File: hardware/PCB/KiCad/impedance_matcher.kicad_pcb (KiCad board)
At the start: 2 copper layers, 72 x 63 mm, 43 parts, among them Q1 PC817, U1 TLV2372IP

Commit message: Small PCB fixes
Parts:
- FAN1, OLED1: footprint Connector:B4B-XH-A -> Project Connectors:B4B-XH-A
- I2C1: footprint Connector:B2B-XH-A -> Project Connectors:B2B-XH-A
- SWR1: footprint Connector:B3B-XH-A -> Project Connectors:B3B-XH-A
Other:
- board text added: "FAN1"
- board text added: "I2C1"
- board text added: "OLED1"
- board text added: "SWR1"

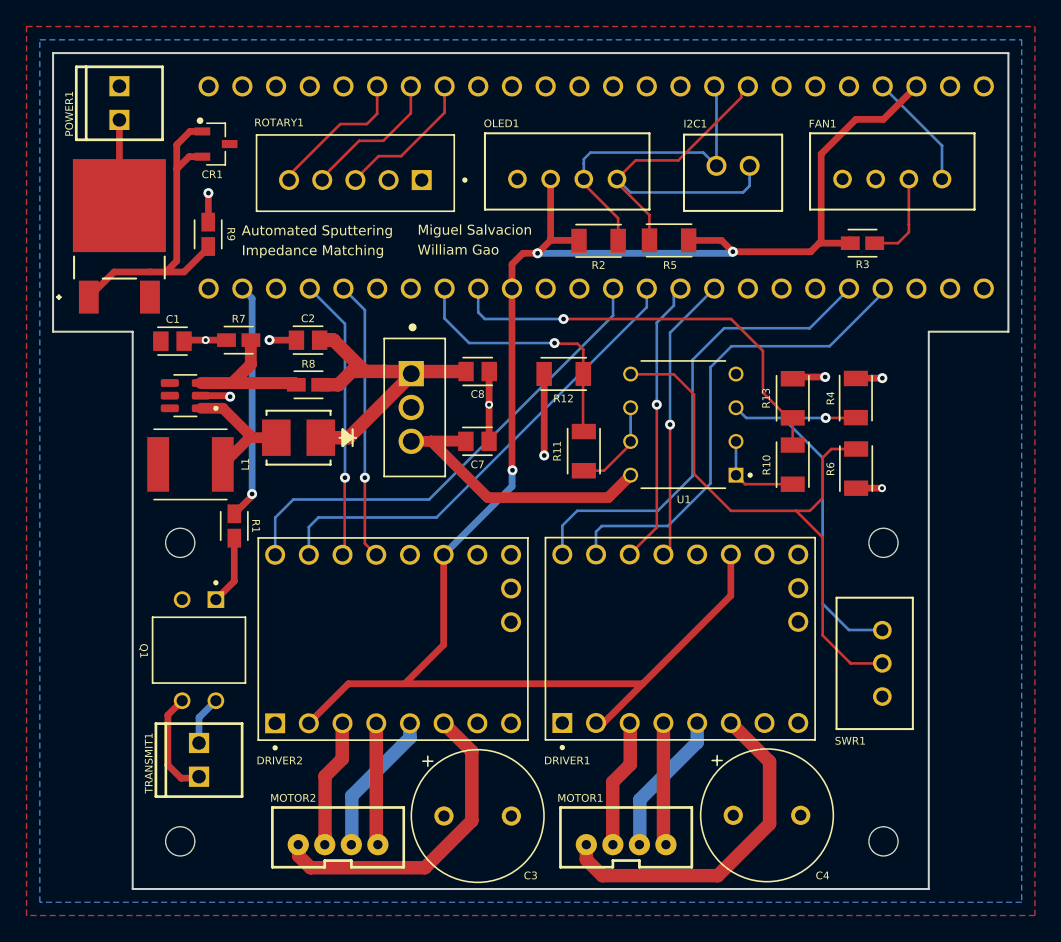
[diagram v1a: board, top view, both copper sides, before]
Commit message: Add some 3D models
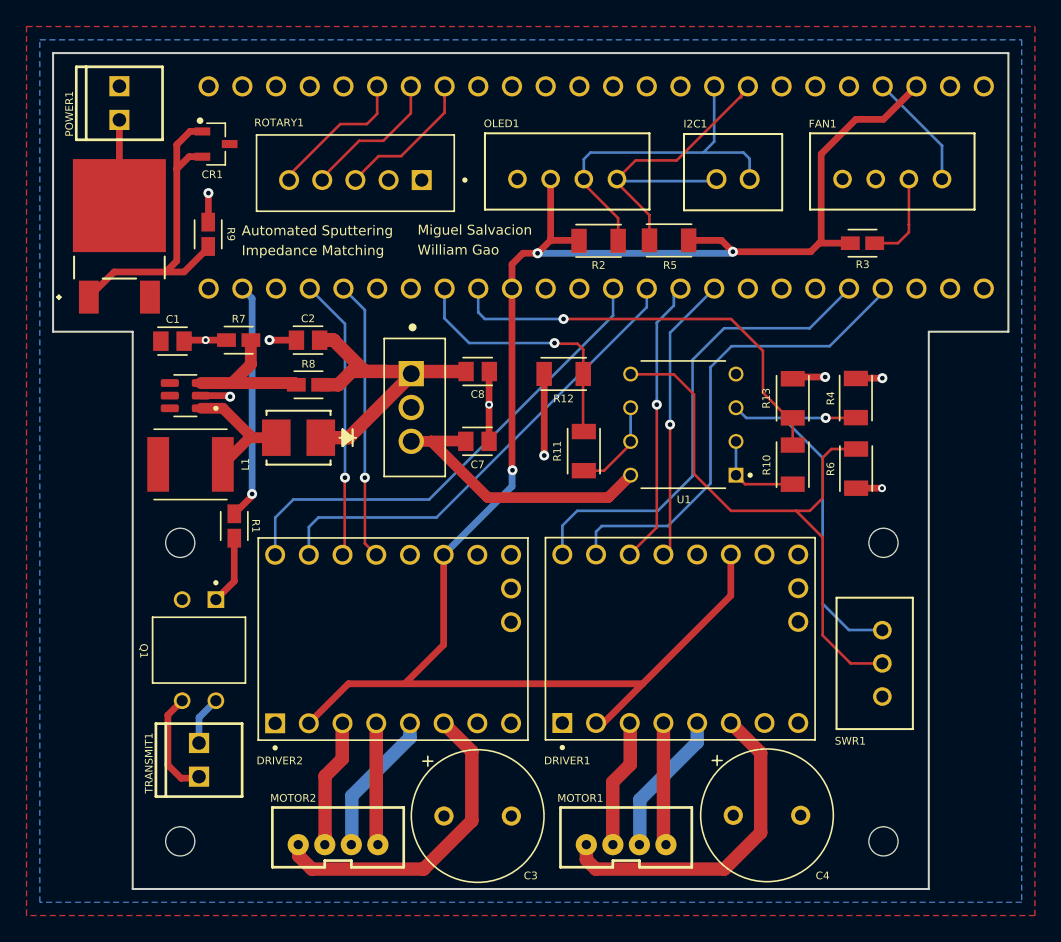
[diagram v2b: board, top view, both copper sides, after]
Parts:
- moved I2C1 2.69 mm to (83.5, 32.0), turned to 180 degrees
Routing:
- net /SCL: track 30.7 -> 26.3 mm
- net /SDA: track 23.9 -> 26.6 mm
- net 18V: track 26.4 -> 25.4 mm
- net Net-(DRIVER1-M2B): track 25.9 -> 24.9 mm
- net GND: track 28.4 -> 27.8 mm
- net Net-(D1-A): track 10.2 -> 9.57 mm
- net Net-(FAN1-Pin_3): track 7.55 -> 6.92 mm
- net Net-(CR1-Pad1): track 25.8 -> 25.1 mm

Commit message: More PCB fixes
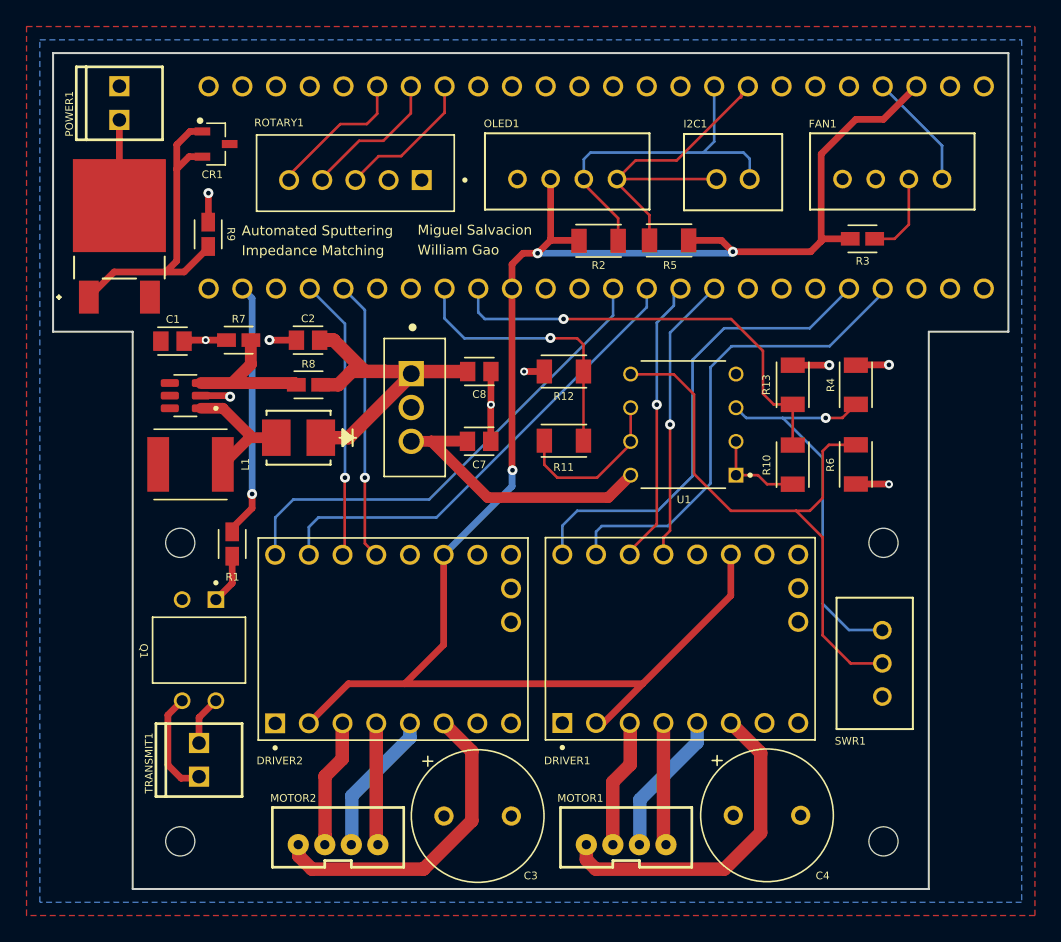
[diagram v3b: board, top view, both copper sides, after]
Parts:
- moved R11 1.69 mm to (69.5, 51.7), turned to 0 degrees
- moved R1 1.37 mm to (44.5, 59.5)
- moved R13 1.02 mm to (86.7, 47.5)
- moved R4 1.00 mm to (91.5, 47.5)
- moved R3 0.33 mm to (92.0, 36.5)
- moved R6 0.32 mm to (91.5, 53.5)
- moved R12 0.18 mm to (69.5, 46.5)
- moved C7 0.12 mm to (63.1, 51.8)
- moved C8 0.12 mm to (63.1, 46.5)
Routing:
- net /IN2: track 6.90 -> 12.3 mm
- net GND: track 27.8 -> 24.6 mm
- net /REV_OUT: track 19.8 -> 20.9 mm
- net Net-(Q1-Pad1): track 5.20 -> 4.06 mm
- net /TRANSMIT: track 17.8 -> 18.9 mm
- net /FWD_OUT: track 32.3 -> 33.3 mm
